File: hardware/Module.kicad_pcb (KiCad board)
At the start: 2 copper layers, 57.5 x 109.2 mm, 32 parts, among them J1 CV_IN_1, J10 GATE_OUT_2, J11 AUDIO_IN_L, J12 AUDIO_IN_R, J13 AUDIO_OUT_L, J14 AUDIO_OUT_R, J15 POWER, J2 CV_IN_2, J3 CV_IN_3, J4 CV_IN_4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

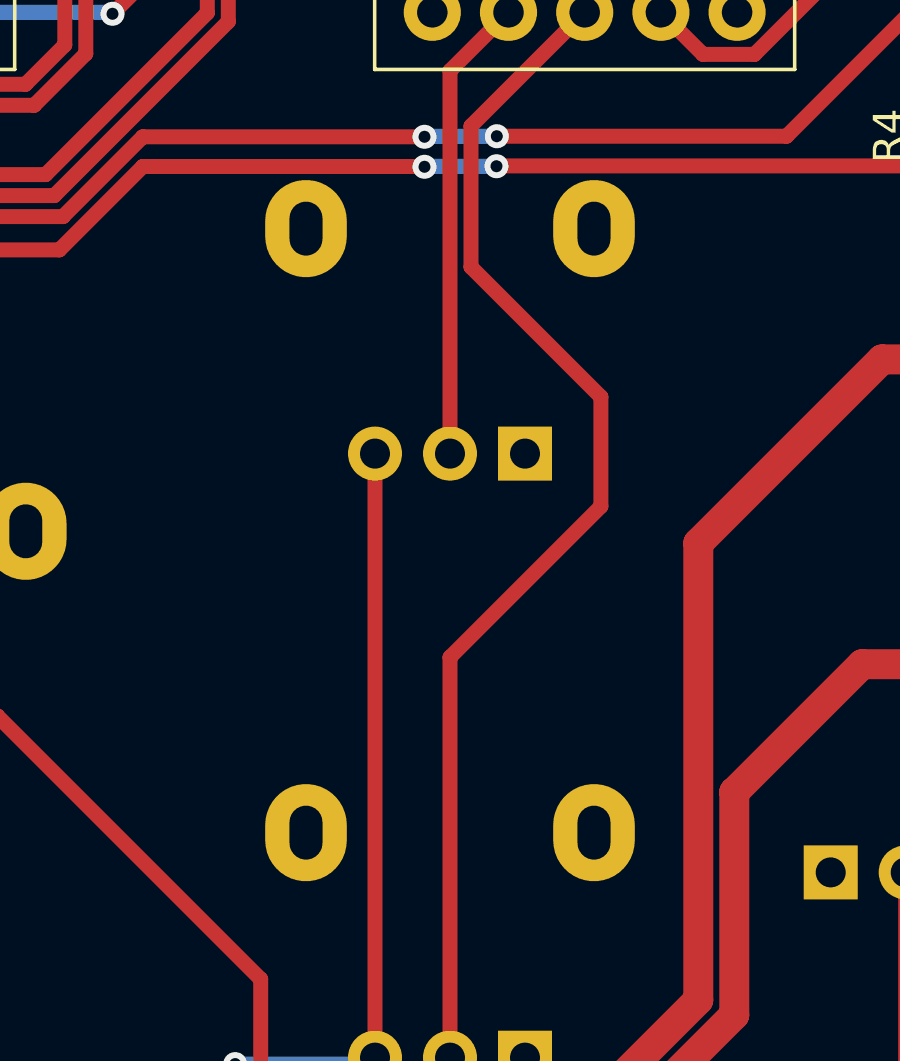
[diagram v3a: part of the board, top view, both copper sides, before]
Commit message: Fix trimmer footprint
Signed-off-by: Petr Horacek <petr@zlosynth.com>
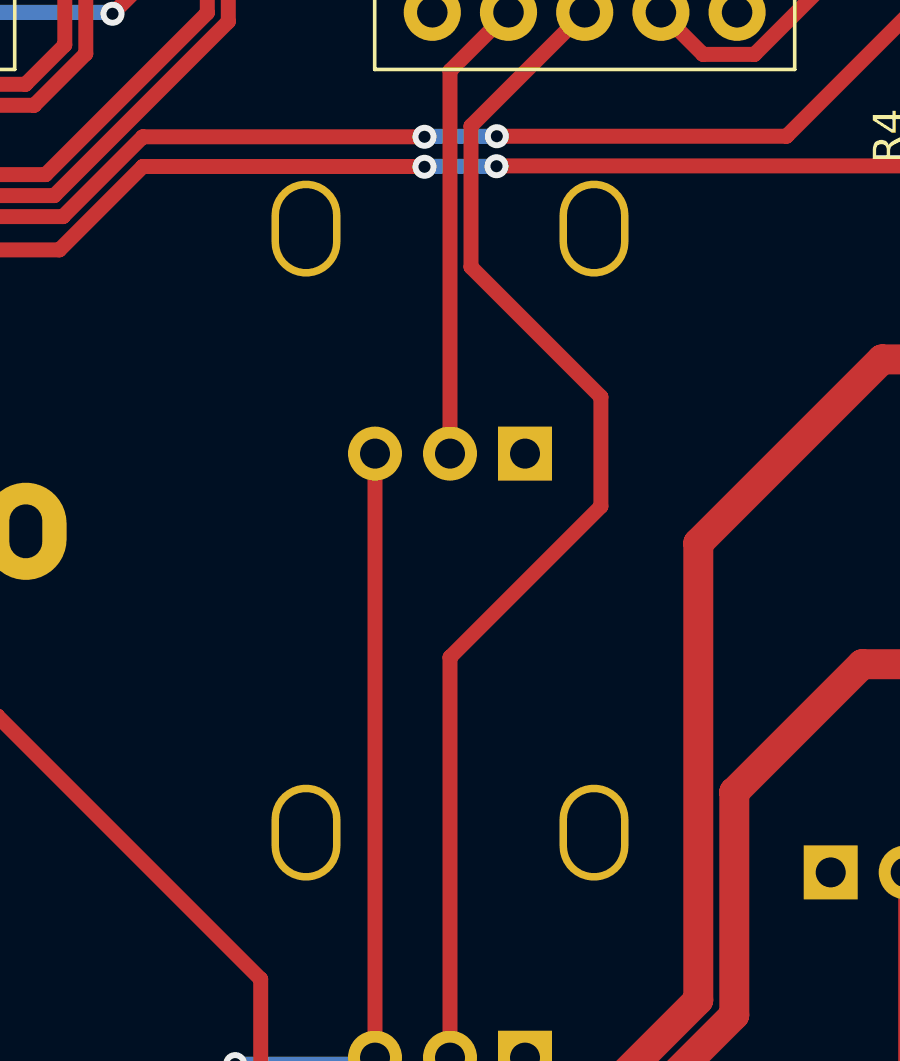
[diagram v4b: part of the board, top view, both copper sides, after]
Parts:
- RV1, RV3: footprint Potentiometer_THT:Potentiometer_Alpha_RD901F-40-00D_Single_Vertical -> Custom:Potentiometer_Thonk_Trimmer
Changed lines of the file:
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@@
     )
   )
-  (footprint "Potentiometer_THT:Potentiometer_Alpha_RD901F-40-00D_Single_Vertical" (layer "B.Cu")
+  (footprint "Custom:Potentiometer_Thonk_Trimmer" (layer "B.Cu")
     (at 80.05 124.955 90)
     (descr "Potentiometer, vertical, 9mm, single, http://www.taiwanalpha.com.tw/downloads?target=products&id=113")
@@
         (effects (font (size 1 1) (thickness 0.15)) (justify mirror))
     )
-    (fp_text value "B10k" (at 0 -9.86 270) (layer "B.Fab")
+    (fp_text value "B10k" (at 5.89 -9.95 270) (layer "B.Fab")
         (effects (font (size 1 1) (thickness 0.15)) (justify mirror))
     )
@@
     (fp_circle (center 7.5 -2.5) (end 7.5 1)
       (stroke (width 0.1) (type solid)) (fill none) (layer "B.Fab"))
-    (pad "" thru_hole oval (at 7.5 -7.3) (size 2.72 3.24) (drill oval 1.1 1.8) (layers "*.Cu" "*.Mask"))
-    (pad "" thru_hole oval (at 7.5 2.3) (size 2.72 3.24) (drill oval 1.1 1.8) (layers "*.Cu" "*.Mask"))
+    (pad "" thru_hole oval (at 7.5 -7.3) (size 2.3 3.2) (drill oval 1.8 2.7) (layers "*.Cu" "*.Mask"))
+    (pad "" thru_hole oval (at 7.5 2.3) (size 2.3 3.2) (drill oval 1.8 2.7) (layers "*.Cu" "*.Mask"))
     (pad "1" thru_hole rect (at 0 0) (size 1.8 1.8) (drill 1) (layers "*.Cu" "*.Mask")
       (net 2 "GND") (pinfunction "1") (pintype "passive"))
@@
     )
   )
-  (footprint "Potentiometer_THT:Potentiometer_Alpha_RD901F-40-00D_Single_Vertical" (layer "B.Cu")
+  (footprint "Custom:Potentiometer_Thonk_Trimmer" (layer "B.Cu")
     (at 80.05 104.82 90)
     (descr "Potentiometer, vertical, 9mm, single, http://www.taiwanalpha.com.tw/downloads?target=products&id=113")
@@
         (effects (font (size 1 1) (thickness 0.15)) (justify mirror))
     )
-    (fp_text value "B10k" (at 0 -9.86 270) (layer "B.Fab")
+    (fp_text value "B10k" (at 5.89 -9.95 270) (layer "B.Fab")
         (effects (font (size 1 1) (thickness 0.15)) (justify mirror))
     )
@@
     (fp_circle (center 7.5 -2.5) (end 7.5 1)
       (stroke (width 0.1) (type solid)) (fill none) (layer "B.Fab"))
-    (pad "" thru_hole oval (at 7.5 -7.3) (size 2.72 3.24) (drill oval 1.1 1.8) (layers "*.Cu" "*.Mask"))
-    (pad "" thru_hole oval (at 7.5 2.3) (size 2.72 3.24) (drill oval 1.1 1.8) (layers "*.Cu" "*.Mask"))
+    (pad "" thru_hole oval (at 7.5 -7.3) (size 2.3 3.2) (drill oval 1.8 2.7) (layers "*.Cu" "*.Mask"))
+    (pad "" thru_hole oval (at 7.5 2.3) (size 2.3 3.2) (drill oval 1.8 2.7) (layers "*.Cu" "*.Mask"))
     (pad "1" thru_hole rect (at 0 0) (size 1.8 1.8) (drill 1) (layers "*.Cu" "*.Mask")
       (net 2 "GND") (pinfunction "1") (pintype "passive"))
